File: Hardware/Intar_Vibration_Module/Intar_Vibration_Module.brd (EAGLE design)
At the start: 17.8 x 25.9 mm, 11 parts, among them J1 GROVE-4P-2.0-3470130P1, SW1 SWITCH_MOMENTARY

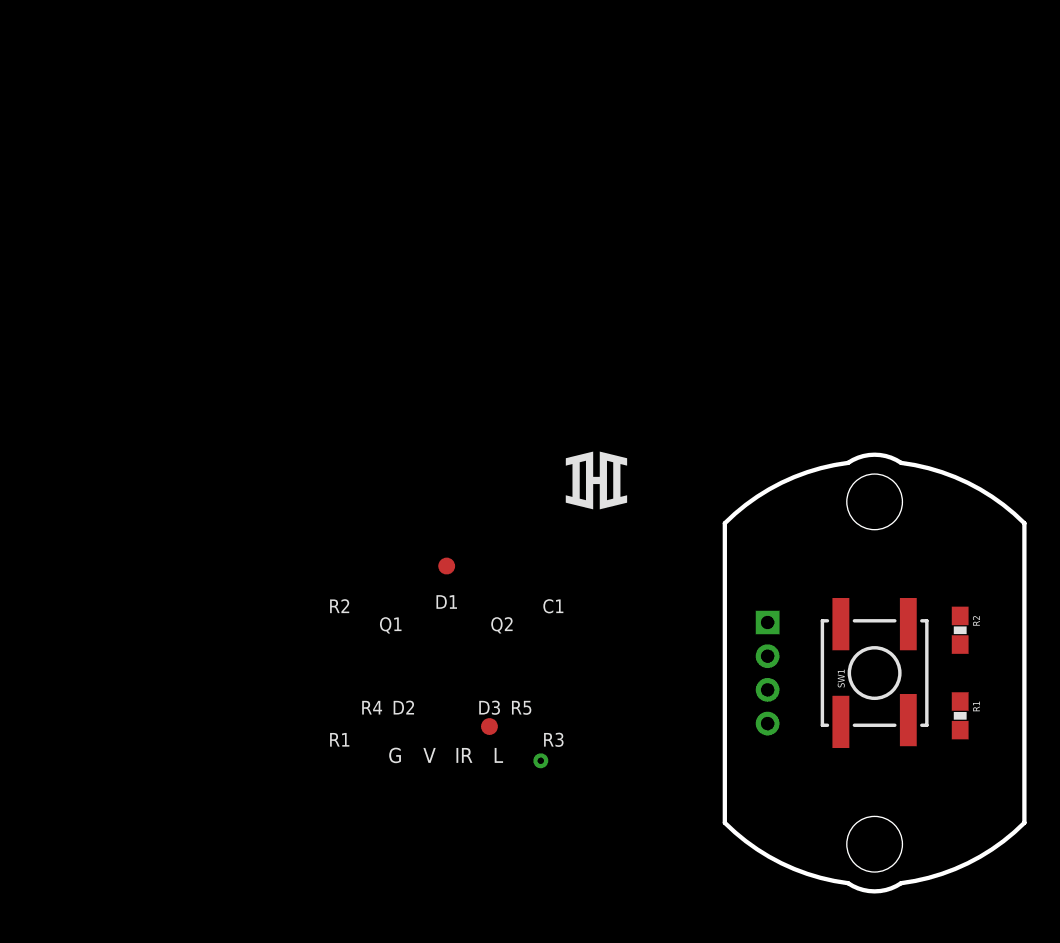
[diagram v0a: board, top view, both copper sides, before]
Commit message: Created schematics for first round of modules.
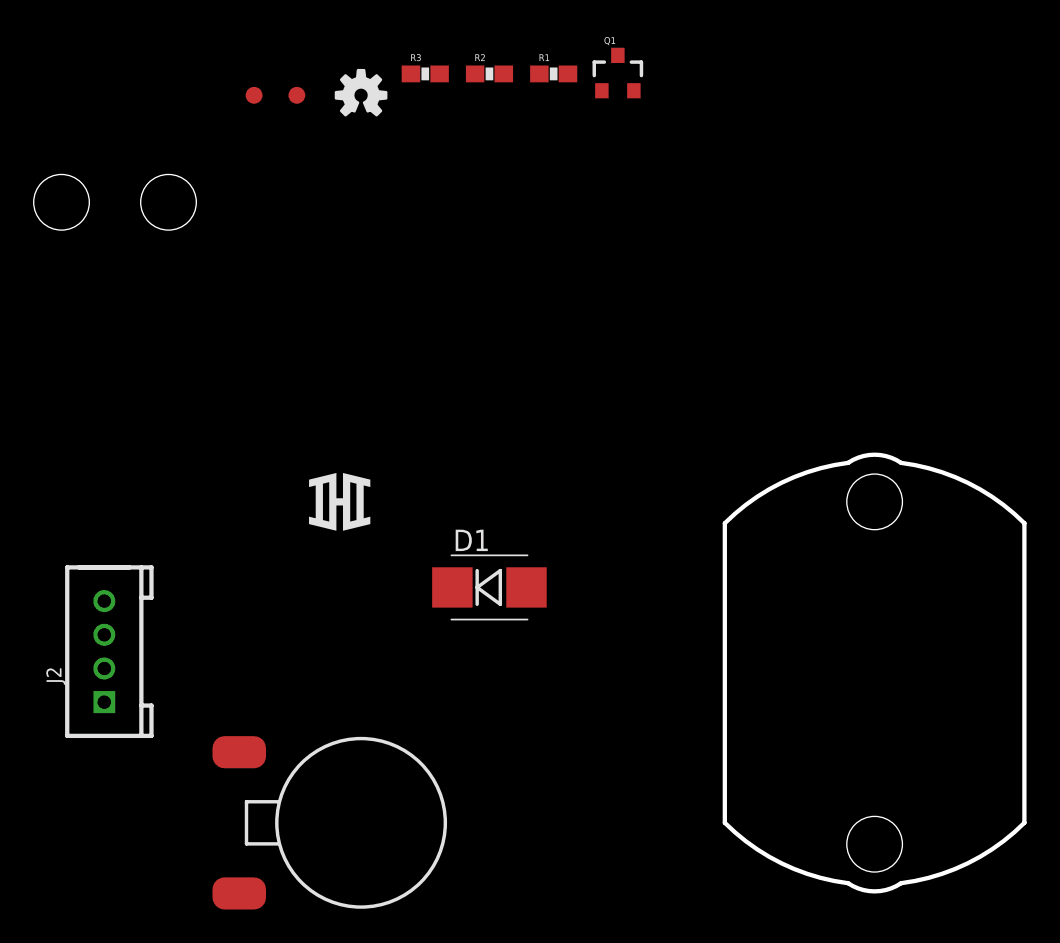
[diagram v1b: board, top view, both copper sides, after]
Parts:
- removed J1: GROVE-4P-2.0-3470130P1, Connector:4P-2.0
- removed SW1: SWITCH_MOMENTARY, Intar_Eagle_Library:KSCXXXG
- added D1: (no value), SparkFun-DiscreteSemi:SMB-DIODE
- added J2: GROVE-4P-2.0-3470130P1, Connector:4P-2.0
- added M1: MOTORVIBE_COIN_SMD, Intar_Eagle_Library:VIBE_COIN_SMD
- added Q1: MMBT2222A, SparkFun-DiscreteSemi:SOT23-3
- added R3: 12, SparkFun-Resistors:0603-RES
- added STANDOFF3, STANDOFF4: STAND-OFF, SparkFun-Electromechanical:STAND-OFF
- R1: value 10K -> 1K
- R2: value 100 -> 100k
- moved FRAME1 79.1 mm to (-101.6, 16.5)
- moved STANDOFF1 56.6 mm to (-41.9, 27.9)
- moved STANDOFF2 51.4 mm to (-48.3, 27.9)
- moved R1 45.1 mm to (-19.1, 35.6), turned to 0 degrees
- moved R2 43.3 mm to (-22.9, 35.6), turned to 0 degrees
- moved LOGO1 41.7 mm to (-30.5, 34.3), flipped to the top
- moved FID2 40.0 mm to (-36.8, 34.3)
- moved FID1 29.3 mm to (-34.3, 34.3)
- moved U$1 15.3 mm to (-31.8, 10.2)
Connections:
- removed net BTN: J1.1, R2.1
- removed net N$1: R1.1, R2.2, SW1.1, SW1.2
- new net N$2: Q1.1, R1.2, R2.2
- new net N$5: Q1.3, R3.1
- new net N$6: D1.A, M1.2, R3.2
- new net SIG: J2.4, R1.1
- net GND: now also J2.1, Q1.2, R2.1; no longer J1.4, SW1.3, SW1.4
- net VCC: now also D1.C, J2.2, M1.1; no longer J1.3, R1.2
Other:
- board text removed: "C1"
- board text removed: "D1"
- board text removed: "D2"
- board text removed: "D3"
- board text removed: "G"
- board text removed: "IR"
- board text removed: "Intar IR LED Module"
- board text removed: "L"
- board text removed: "Q1"
- board text removed: "Q2"
- board text removed: "R1"
- board text removed: "R2"
- board text removed: "R3"
- board text removed: "R4"
- board text removed: "R5"
- board text removed: "Shawn Hymel"
- board text removed: "V"
- board text removed: "Visible LEDs"
- board text removed: "v01"

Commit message: Arranged components on all modules
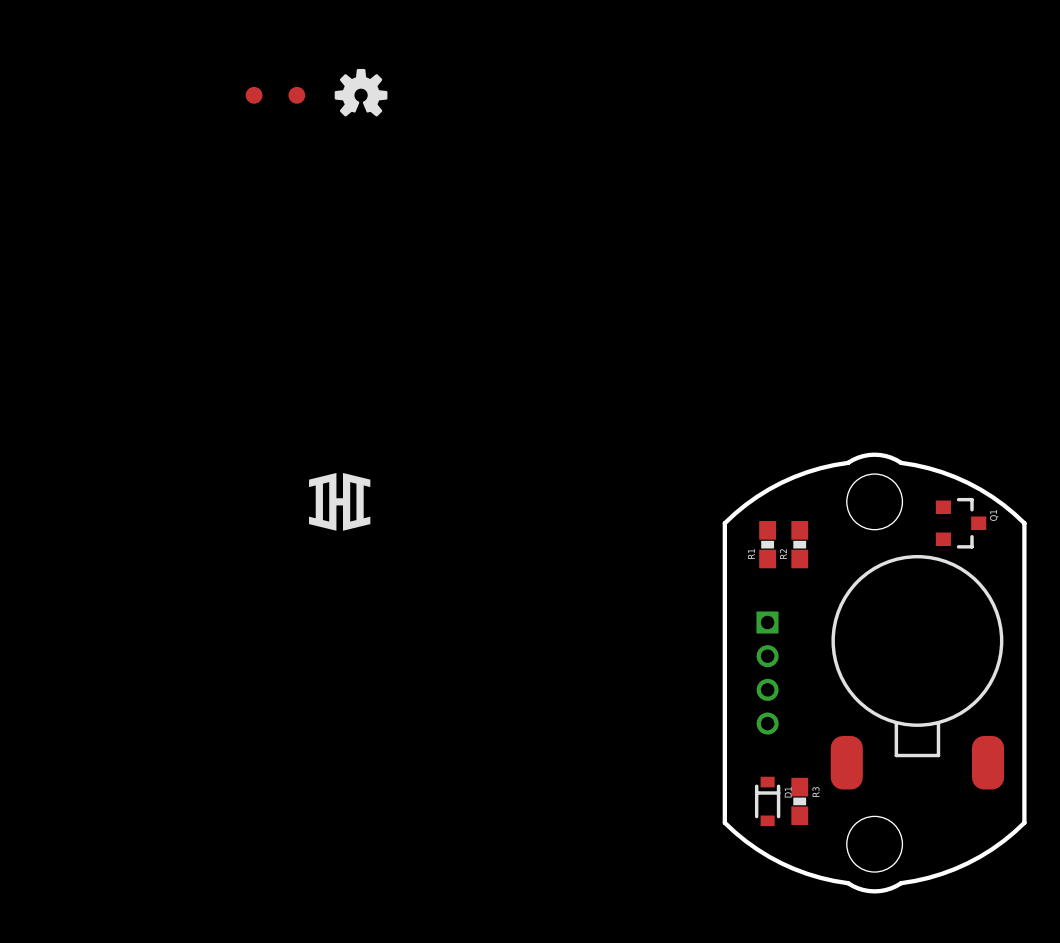
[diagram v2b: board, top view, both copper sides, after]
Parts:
- removed STANDOFF3, STANDOFF4: STAND-OFF, SparkFun-Electromechanical:STAND-OFF
- D1: value (none) -> 250mA/100V; device SparkFun-DiscreteSemi:SMB-DIODE -> SparkFun-DiscreteSemi:SOD-323
- moved STANDOFF2 61.5 mm to (0.00, -10.2)
- moved R3 48.6 mm to (-4.45, -7.62), turned to 270 degrees
- moved STANDOFF1 45.5 mm to (0.00, 10.2)
- moved J2 39.4 mm to (-6.35, 0.00), flipped to the bottom, turned to 270 degrees
- moved M1 34.7 mm to (2.54, 1.91), turned to 0 degrees
- moved Q1 33.5 mm to (5.08, 8.89), turned to 270 degrees
- moved R2 33.5 mm to (-4.45, 7.62), turned to 90 degrees
- moved R1 30.7 mm to (-6.35, 7.62), turned to 90 degrees
- moved D1 20.8 mm to (-6.35, -7.62), turned to 270 degrees
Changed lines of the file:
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@@
 <setting verticaltext="up"/>
 </settings>
-<grid distance="0.05" unitdist="inch" unit="inch" style="lines" multiple="1" display="yes" altdistance="0.005" altunitdist="inch" altunit="inch"/>
+<grid distance="0.05" unitdist="inch" unit="inch" style="dots" multiple="1" display="yes" altdistance="0.025" altunitdist="inch" altunit="inch"/>
 <layers>
 <layer number="1" name="Top" color="4" fill="1" visible="yes" active="yes"/>
 <layer number="2" name="Route2" color="1" fill="3" visible="no" active="yes"/>
 <layer number="15" name="Route15" color="4" fill="6" visible="no" active="yes"/>
-<layer number="16" name="Bottom" color="1" fill="1" visible="yes" active="yes"/>
+<layer number="16" name="Bottom" color="1" fill="1" visible="no" active="yes"/>
 <layer number="17" name="Pads" color="2" fill="1" visible="yes" active="yes"/>
 <layer number="18" name="Vias" color="2" fill="1" visible="yes" active="yes"/>
@@
 <layer number="20" name="Dimension" color="15" fill="1" visible="yes" active="yes"/>
 <layer number="21" name="tPlace" color="16" fill="1" visible="yes" active="yes"/>
-<layer number="22" name="bPlace" color="14" fill="1" visible="yes" active="yes"/>
+<layer number="22" name="bPlace" color="14" fill="1" visible="no" active="yes"/>
 <layer number="23" name="tOrigins" color="15" fill="1" visible="yes" active="yes"/>
-<layer number="24" name="bOrigins" color="15" fill="1" visible="yes" active="yes"/>
+<layer number="24" name="bOrigins" color="15" fill="1" visible="no" active="yes"/>
 <layer number="25" name="tNames" color="7" fill="1" visible="no" active="yes"/>
 <layer number="26" name="bNames" color="7" fill="1" visible="no" active="yes"/>
@@
 <layer number="43" name="vRestrict" color="2" fill="10" visible="no" active="yes"/>
 <layer number="44" name="Drills" color="7" fill="1" visible="no" active="yes"/>
-<layer number="45" name="Holes" color="7" fill="1" visible="yes" active="yes"/>
+<layer number="45" name="Holes" color="7" fill="1" visible="no" active="yes"/>
 <layer number="46" name="Milling" color="3" fill="1" visible="no" active="yes"/>
 <layer number="47" name="Measures" color="7" fill="1" visible="no" active="yes"/>
-<layer number="51" name="tDocu" color="6" fill="1" visible="yes" active="yes"/>
+<layer number="51" name="tDocu" color="6" fill="1" visible="no" active="yes"/>
 <layer number="52" name="bDocu" color="7" fill="1" visible="no" active="yes"/>
 <layer number="3" name="Route3" color="4" fill="3" visible="no" active="no"/>
@@
 </autorouter>
 <elements>
-<element name="D1" library="SparkFun-DiscreteSemi" package="SMB-DIODE" value="" x="-22.86" y="5.08">
-<attribute name="PROD_ID" value="DIO-09646" x="-22.86" y="5.08" size="1.778" layer="27" display="off"/>
+<element name="D1" library="SparkFun-DiscreteSemi" package="SOD-323" value="250mA/100V" x="-6.35" y="-7.62" rot="R270">
+<attribute name="PROD_ID" value="DIO-09646" x="-6.35" y="-7.62" size="1.778" layer="27" rot="R270" display="off"/>
+<attribute name="VALUE" value="250mA/100V" x="-6.35" y="-7.62" size="1.778" layer="27" rot="R270" display="off"/>
 </element>
 <element name="FID1" library="SparkFun-Aesthetics" package="FIDUCIAL-1X2" value="FIDUCIAL1X2" x="-34.29" y="34.29"/>
 <element name="FID2" library="SparkFun-Aesthetics" package="FIDUCIAL-1X2" value="FIDUCIAL1X2" x="-36.83" y="34.29"/>
 <element name="FRAME1" library="SparkFun-Aesthetics" package="CREATIVE_COMMONS" value="FRAME-LETTER" x="-101.6" y="16.51"/>
-<element name="J2" library="Connector" package="4P-2.0" value="GROVE-4P-2.0-3470130P1" x="-45.72" y="1.27" rot="R90"/>
+<element name="J2" library="Connector" package="4P-2.0" value="GROVE-4P-2.0-3470130P1" x="-6.35" y="0" rot="MR270"/>
 <element name="LOGO1" library="SparkFun-Aesthetics" package="OSHW-LOGO-S" value="OSHW-LOGOS" x="-30.48" y="34.29"/>
-<element name="M1" library="Intar_Eagle_Library" package="VIBE_COIN_SMD" value="MOTORVIBE_COIN_SMD" x="-30.48" y="-8.89" rot="R270"/>
-<element name="Q1" library="SparkFun-DiscreteSemi" package="SOT23-3" value="MMBT2222A" x="-15.24" y="35.56">
-<attribute name="PROD_ID" value="TRANS-08049" x="-15.24" y="35.56" size="1.778" layer="27" display="off"/>
+<element name="M1" library="Intar_Eagle_Library" package="VIBE_COIN_SMD" value="MOTORVIBE_COIN_SMD" x="2.54" y="1.905"/>
+<element name="Q1" library="SparkFun-DiscreteSemi" package="SOT23-3" value="MMBT2222A" x="5.08" y="8.89" rot="R270">
+<attribute name="PROD_ID" value="TRANS-08049" x="5.08" y="8.89" size="1.778" layer="27" rot="R270" display="off"/>
 </element>
-<element name="R1" library="SparkFun-Resistors" package="0603-RES" value="1K" x="-19.05" y="35.56">
-<attribute name="PROD_ID" value="RES-07856" x="-19.05" y="35.56" size="1.778" layer="27" display="off"/>
+<element name="R1" library="SparkFun-Resistors" package="0603-RES" value="1K" x="-6.35" y="7.62" rot="R90">
+<attribute name="PROD_ID" value="RES-07856" x="-6.35" y="7.62" size="1.778" layer="27" rot="R90" display="off"/>
 </element>
-<element name="R2" library="SparkFun-Resistors" package="0603-RES" value="100k" x="-22.86" y="35.56">
-<attribute name="PROD_ID" value="RES-07828" x="-22.86" y="35.56" size="1.778" layer="27" display="off"/>
+<element name="R2" library="SparkFun-Resistors" package="0603-RES" value="100k" x="-4.445" y="7.62" rot="R90">
+<attribute name="PROD_ID" value="RES-07828" x="-4.445" y="7.62" size="1.778" layer="27" rot="R90" display="off"/>
 </element>
-<element name="R3" library="SparkFun-Resistors" package="0603-RES" value="12" x="-26.67" y="35.56"/>
-<element name="STANDOFF1" library="SparkFun-Electromechanical" package="STAND-OFF" value="STAND-OFF" x="-41.91" y="27.94"/>
-<element name="STANDOFF2" library="SparkFun-Electromechanical" package="STAND-OFF" value="STAND-OFF" x="-48.26" y="27.94"/>
-<element name="STANDOFF3" library="SparkFun-Electromechanical" package="STAND-OFF" value="STAND-OFF" x="0" y="-10.16"/>
-<element name="STANDOFF4" library="SparkFun-Electromechanical" package="STAND-OFF" value="STAND-OFF" x="0" y="10.16"/>
+<element name="R3" library="SparkFun-Resistors" package="0603-RES" value="12" x="-4.445" y="-7.62" rot="R270"/>
+<element name="STANDOFF1" library="SparkFun-Electromechanical" package="STAND-OFF" value="STAND-OFF" x="0" y="10.16"/>
+<element name="STANDOFF2" library="SparkFun-Electromechanical" package="STAND-OFF" value="STAND-OFF" x="0" y="-10.16"/>
 <element name="U$1" library="Intar_Eagle_Library" package="LOGO_SM" value="LOGOSM" x="-31.75" y="10.16"/>
 </elements>
@@
 <contactref element="R2" pad="1"/>
 <contactref element="Q1" pad="2"/>
-<wire x1="-23.71" y1="35.56" x2="-14.29" y2="34.56" width="0" layer="19" extent="1-1"/>
-<wire x1="-45.72" y1="-1.73" x2="-23.71" y2="35.56" width="0" layer="19" extent="1-1"/>
+<wire x1="-6.35" y1="3" x2="-4.445" y2="6.77" width="0" layer="19" extent="1-1"/>
+<wire x1="4.08" y1="7.94" x2="-6.35" y2="3" width="0" layer="19" extent="1-1"/>
 </signal>
 <signal name="VCC">
@@
 <contactref element="D1" pad="C"/>
 <contactref element="M1" pad="1"/>
-<wire x1="-45.72" y1="0.27" x2="-25.06" y2="5.08" width="0" layer="19" extent="1-1"/>
-<wire x1="-37.709" y1="-13.081" x2="-45.72" y2="0.27" width="0" layer="19" extent="1-1"/>
+<wire x1="-6.35" y1="1" x2="-6.35" y2="-6.47" width="0" layer="19" extent="1-1"/>
+<wire x1="6.731" y1="-5.324" x2="-6.35" y2="-6.47" width="0" layer="19" extent="1-1"/>
 </signal>
 <signal name="SIG">
 <contactref element="J2" pad="4"/>
 <contactref element="R1" pad="1"/>
-<wire x1="-45.72" y1="4.27" x2="-19.9" y2="35.56" width="0" layer="19" extent="1-1"/>
+<wire x1="-6.35" y1="-3" x2="-6.35" y2="6.77" width="0" layer="19" extent="1-1"/>
 </signal>
 <signal name="N$2">
@@
 <contactref element="Q1" pad="1"/>
 <contactref element="R2" pad="2"/>
-<wire x1="-16.19" y1="34.56" x2="-18.2" y2="35.56" width="0" layer="19" extent="1-1"/>
-<wire x1="-22.01" y1="35.56" x2="-18.2" y2="35.56" width="0" layer="19" extent="1-1"/>
+<wire x1="4.08" y1="9.84" x2="-6.35" y2="8.47" width="0" layer="19" extent="1-1"/>
+<wire x1="-4.445" y1="8.47" x2="4.08" y2="9.84" width="0" layer="19" extent="1-1"/>
 </signal>
 <signal name="N$5">
 <contactref element="Q1" pad="3"/>
 <contactref element="R3" pad="1"/>
-<wire x1="-27.52" y1="35.56" x2="-15.24" y2="36.66" width="0" layer="19" extent="1-1"/>
+<wire x1="6.18" y1="8.89" x2="-4.445" y2="-6.77" width="0" layer="19" extent="1-1"/>
 </signal>
 <signal name="N$6">
@@
 <contactref element="M1" pad="2"/>
 <contactref element="D1" pad="A"/>
-<wire x1="-20.66" y1="5.08" x2="-37.709" y2="-4.699" width="0" layer="19" extent="1-1"/>
-<wire x1="-25.82" y1="35.56" x2="-20.66" y2="5.08" width="0" layer="19" extent="1-1"/>
+<wire x1="-6.35" y1="-8.77" x2="-4.445" y2="-8.47" width="0" layer="19" extent="1-1"/>
+<wire x1="-1.651" y1="-5.324" x2="-4.445" y2="-8.47" width="0" layer="19" extent="1-1"/>
 </signal>
 </signals>
